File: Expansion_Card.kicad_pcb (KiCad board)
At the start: 4 copper layers, 26 x 30 mm, 38 parts, among them J1 Conn_01x03_MountingPin, J2 Conn_01x03_MountingPin, P1 USB_C_Plug_USB2.0, SW1 SW_Push, SW2 SW_Push, U1 AP2112K-3.3, U2 RP2354A, Y1 ABM8-272-T3

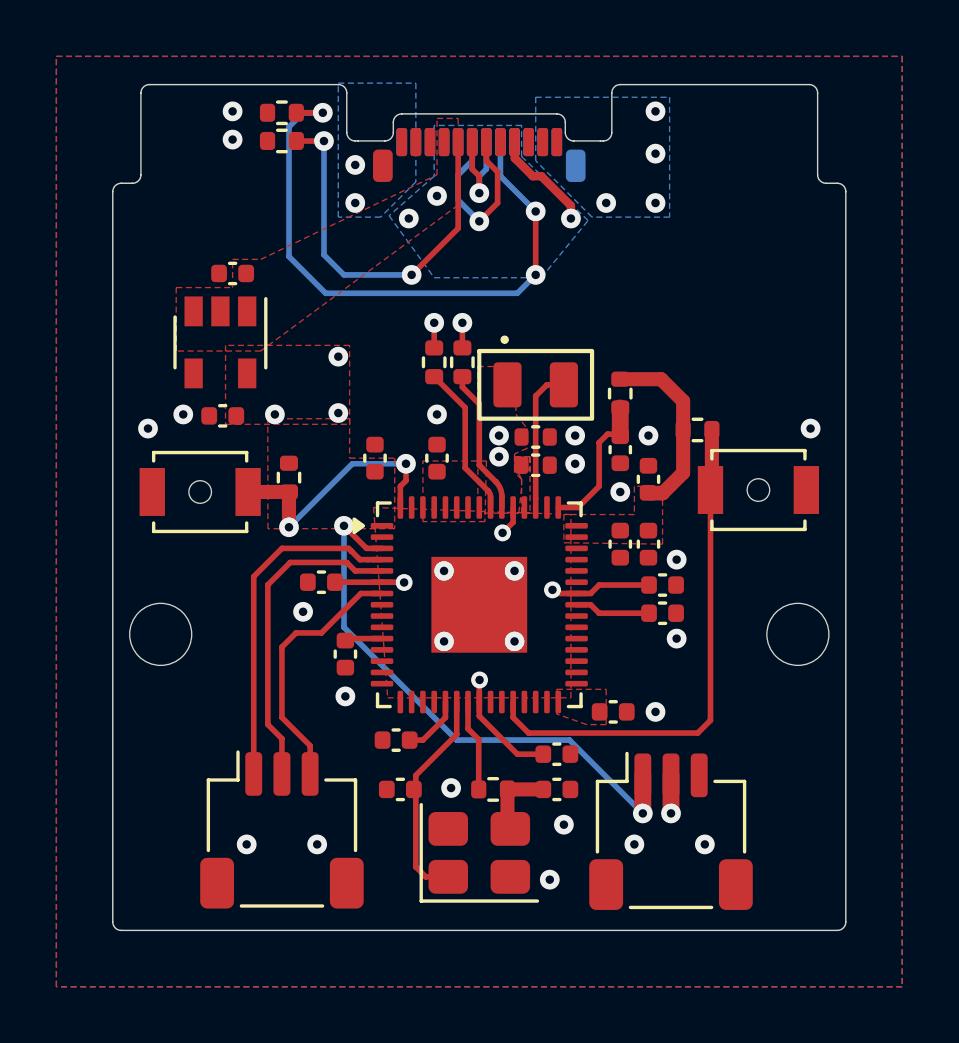
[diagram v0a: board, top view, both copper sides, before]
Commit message: add fiducials/testpoints
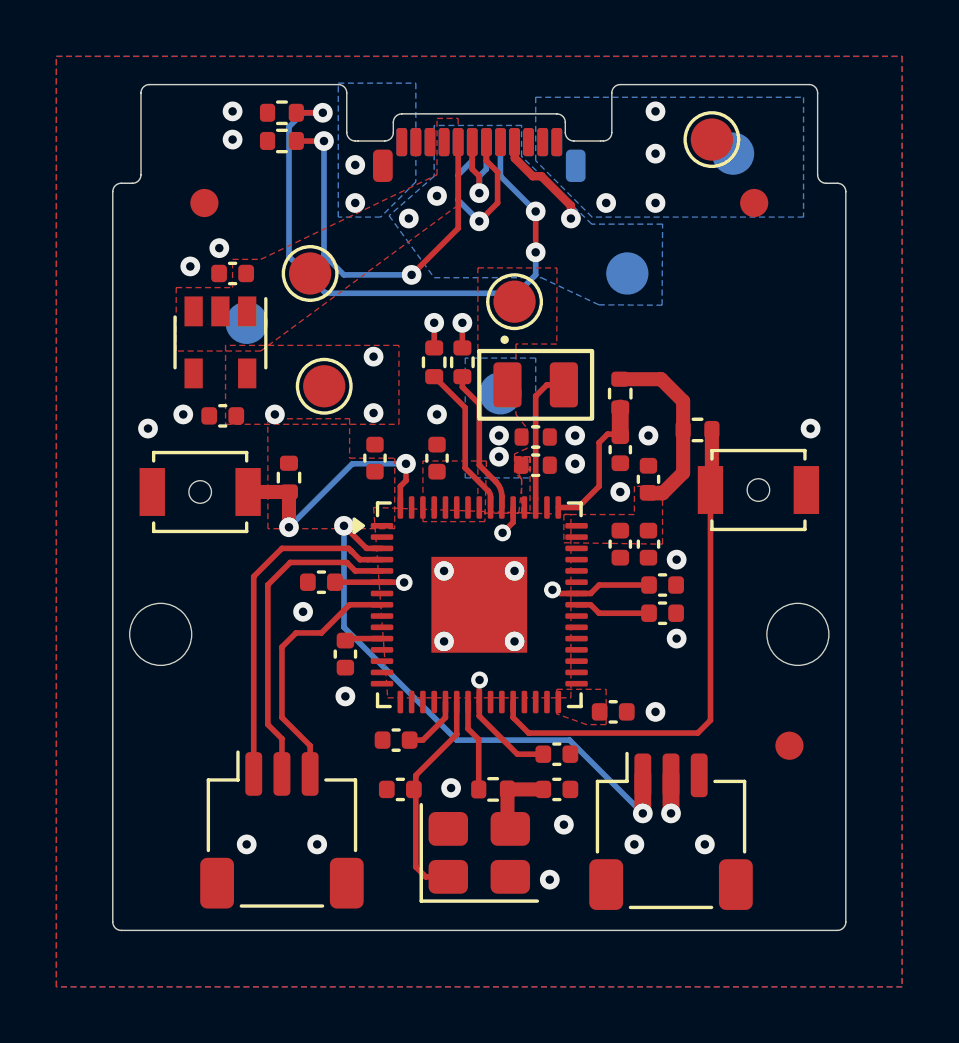
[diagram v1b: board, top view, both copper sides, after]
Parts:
- added FID1: Fiducial, Fiducial:Fiducial_1mm_Mask2mm, F.Cu at (130.2, 131.2)
- added FID2: Fiducial, Fiducial:Fiducial_1mm_Mask2mm, F.Cu at (149.8, 131.2)
- added FID3: Fiducial, Fiducial:Fiducial_1mm_Mask2mm, F.Cu at (151.0, 150.4)
- added TP1: TestPoint, TestPoint:TestPoint_Pad_D1.5mm, B.Cu at (131.8, 135.4)
- added TP2: TestPoint, TestPoint:TestPoint_Pad_D1.5mm, B.Cu at (145.2, 133.7)
- added TP3: TestPoint, TestPoint:TestPoint_Pad_D1.5mm, B.Cu at (149.0, 129.4)
- added TP4: TestPoint, TestPoint:TestPoint_Pad_D1.5mm, B.Cu at (140.8, 137.9)
- added TP5: TestPoint, TestPoint:TestPoint_Pad_D1.5mm, F.Cu at (148.2, 128.9)
- added TP6: TestPoint, TestPoint:TestPoint_Pad_D1.5mm, F.Cu at (134.0, 133.7)
- added TP7: TestPoint, TestPoint:TestPoint_Pad_D1.5mm, F.Cu at (134.5, 137.7)
- added TP8: TestPoint, TestPoint:TestPoint_Pad_D1.5mm, F.Cu at (141.2, 134.7)
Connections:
- U2 pad 7: /SWO -> unconnected-(U2-GPIO4-Pad7)
- U2 pad 8: unconnected-(U2-GPIO5-Pad8) -> /SWO
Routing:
- net GND: vias 32 -> 34
- added copper zone on B.Cu, net +1V1
